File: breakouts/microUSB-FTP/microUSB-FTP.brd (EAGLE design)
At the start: 13.6 x 14.2 mm, 8 parts, among them X1 USB-MICROB

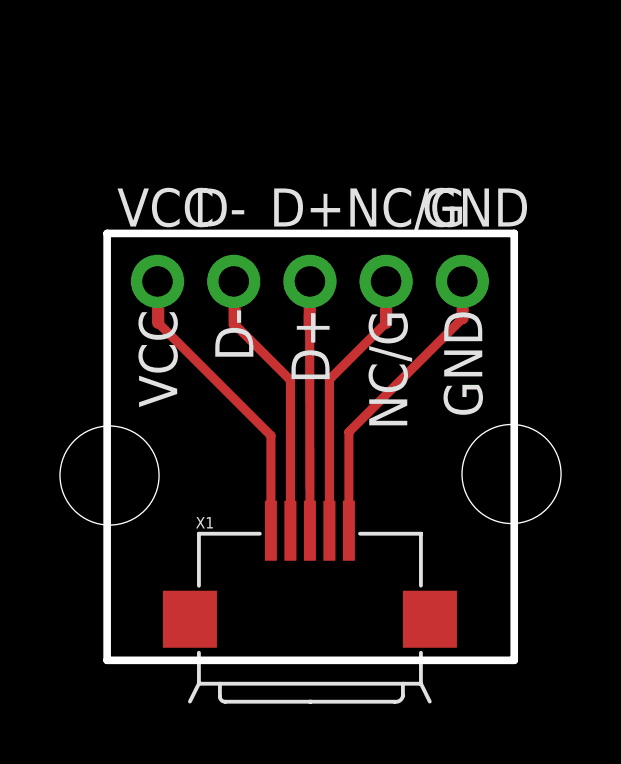
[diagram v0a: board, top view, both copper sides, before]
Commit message: microUSB FTP mid-point footprint
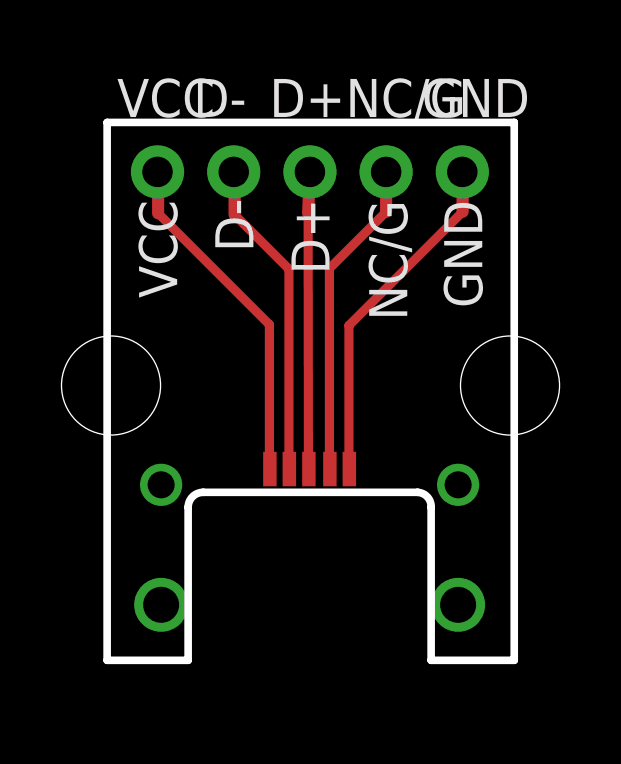
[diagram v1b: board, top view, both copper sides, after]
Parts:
- removed X1: USB-MICROB, SparkFun:USB-MICROB
- moved D+ 3.65 mm to (10.2, 16.3)
- moved D- 3.65 mm to (7.62, 16.3)
- moved GND 3.65 mm to (15.2, 16.3)
- moved NC/G 3.65 mm to (12.7, 16.3)
- moved VCC 3.65 mm to (5.08, 16.3)
- moved JP4 3.00 mm to (3.53, 9.21)
- moved JP3 2.95 mm to (16.8, 9.21)
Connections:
- net D+: no longer X1.D+
- net D-: no longer X1.D-
- net GND: no longer X1.GND
- net S$1: no longer X1.ID
- net VBUS: no longer X1.VBUS
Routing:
- net D+: track 8.31 -> 9.51 mm
- net D-: track 9.09 -> 10.3 mm
- net GND: track 9.88 -> 11.0 mm
- net S$1: track 9.09 -> 10.2 mm
- net VBUS: track 9.88 -> 11.0 mm
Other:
- board size 13.6 x 14.2 mm -> 13.6 x 17.9 mm
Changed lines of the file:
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@@
 <board>
 <plain>
-<wire x1="3.4" y1="0.05" x2="3.4" y2="14.28" width="0.254" layer="20"/>
-<wire x1="3.4" y1="14.28" x2="16.97" y2="14.28" width="0.254" layer="20"/>
-<wire x1="16.97" y1="14.28" x2="16.97" y2="0.05" width="0.254" layer="20"/>
-<wire x1="16.97" y1="0.05" x2="3.4" y2="0.05" width="0.254" layer="20"/>
-<text x="14.635" y="11.74" size="1.27" layer="121" font="vector" ratio="15" rot="R270">GND</text>
-<text x="9.545" y="11.79" size="1.27" layer="121" font="vector" ratio="15" rot="R270">D+</text>
-<text x="7.005" y="11.79" size="1.27" layer="121" font="vector" ratio="15" rot="R270">D-</text>
-<text x="4.465" y="11.74" size="1.27" layer="121" font="vector" ratio="15" rot="R270">VCC</text>
-<text x="12.135" y="11.74" size="1.27" layer="121" font="vector" ratio="15" rot="R270">NC/G</text>
-<text x="15" y="9.55" size="1.27" layer="122" font="vector" rot="MR0">quilix.com</text>
+<wire x1="3.4" y1="0.05" x2="3.4" y2="17.98" width="0.254" layer="20"/>
+<wire x1="3.4" y1="17.98" x2="16.97" y2="17.98" width="0.254" layer="20"/>
+<wire x1="16.97" y1="17.98" x2="16.97" y2="0.05" width="0.254" layer="20"/>
+<wire x1="16.97" y1="0.05" x2="14.2" y2="0.05" width="0.254" layer="20"/>
+<wire x1="14.2" y1="0.05" x2="14.2" y2="5.15" width="0.254" layer="20"/>
+<wire x1="14.2" y1="5.15" x2="13.75" y2="5.65" width="0.254" layer="20" curve="90"/>
+<wire x1="13.75" y1="5.65" x2="6.6" y2="5.65" width="0.254" layer="20"/>
+<wire x1="6.6" y1="5.65" x2="6.1" y2="5.15" width="0.254" layer="20" curve="90"/>
+<wire x1="6.1" y1="5.15" x2="6.1" y2="0.05" width="0.254" layer="20"/>
+<wire x1="6.1" y1="0.05" x2="3.4" y2="0.05" width="0.254" layer="20"/>
+<text x="14.635" y="15.39" size="1.27" layer="121" font="vector" ratio="15" rot="R270">GND</text>
+<text x="9.545" y="15.44" size="1.27" layer="121" font="vector" ratio="15" rot="R270">D+</text>
+<text x="7.005" y="15.44" size="1.27" layer="121" font="vector" ratio="15" rot="R270">D-</text>
+<text x="4.465" y="15.39" size="1.27" layer="121" font="vector" ratio="15" rot="R270">VCC</text>
+<text x="12.135" y="15.39" size="1.27" layer="121" font="vector" ratio="15" rot="R270">NC/G</text>
+<text x="14.85" y="12.95" size="1.27" layer="122" font="vector" rot="MR0">quilix.com</text>
+<rectangle x1="8.6" y1="5.85" x2="9.05" y2="7" layer="1"/>
+<rectangle x1="9.25" y1="5.85" x2="9.7" y2="7" layer="1"/>
+<rectangle x1="9.9" y1="5.85" x2="10.35" y2="7" layer="1"/>
+<rectangle x1="10.6" y1="5.85" x2="11.05" y2="7" layer="1"/>
+<rectangle x1="11.25" y1="5.85" x2="11.7" y2="7" layer="1"/>
+<rectangle x1="8.55" y1="5.8" x2="9.1" y2="7.05" layer="29"/>
+<rectangle x1="9.2" y1="5.8" x2="9.75" y2="7.05" layer="29"/>
+<rectangle x1="9.85" y1="5.8" x2="10.4" y2="7.05" layer="29"/>
+<rectangle x1="10.55" y1="5.8" x2="11.1" y2="7.05" layer="29"/>
+<rectangle x1="11.2" y1="5.8" x2="11.75" y2="7.05" layer="29"/>
 </plain>
 <attributes>
@@
 </autorouter>
 <elements>
-<element name="X1" library="SparkFun" package="USB-MICROB" value="USB-MICROB" x="10.16" y="1.27"/>
-<element name="JP3" library="SparkFun" package="STAND-OFF" value="STAND-OFF" x="16.88" y="6.26"/>
-<element name="JP4" library="SparkFun" package="STAND-OFF" value="STAND-OFF" x="3.48" y="6.21"/>
-<element name="VCC" library="adafruit" package="1X01-CLEANBIG" value="" x="5.08" y="12.68"/>
-<element name="D-" library="adafruit" package="1X01-CLEANBIG" value="" x="7.62" y="12.68"/>
-<element name="D+" library="adafruit" package="1X01-CLEANBIG" value="" x="10.16" y="12.68"/>
-<element name="NC/G" library="adafruit" package="1X01-CLEANBIG" value="" x="12.7" y="12.68"/>
-<element name="GND" library="adafruit" package="1X01-CLEANBIG" value="" x="15.24" y="12.68"/>
+<element name="JP3" library="SparkFun" package="STAND-OFF" value="STAND-OFF" x="16.83" y="9.21"/>
+<element name="JP4" library="SparkFun" package="STAND-OFF" value="STAND-OFF" x="3.53" y="9.21"/>
+<element name="VCC" library="adafruit" package="1X01-CLEANBIG" value="" x="5.08" y="16.33"/>
+<element name="D-" library="adafruit" package="1X01-CLEANBIG" value="" x="7.62" y="16.33"/>
+<element name="D+" library="adafruit" package="1X01-CLEANBIG" value="" x="10.16" y="16.33"/>
+<element name="NC/G" library="adafruit" package="1X01-CLEANBIG" value="" x="12.7" y="16.33"/>
+<element name="GND" library="adafruit" package="1X01-CLEANBIG" value="" x="15.24" y="16.33"/>
 </elements>
 <signals>
 <signal name="GND">
-<contactref element="X1" pad="GND"/>
 <contactref element="GND" pad="1"/>
-<wire x1="15.24" y1="12.68" x2="15.25" y2="12.67" width="0.4064" layer="1"/>
-<wire x1="15.25" y1="12.67" x2="15.25" y2="11.45" width="0.4064" layer="1"/>
-<wire x1="15.25" y1="11.45" x2="11.46" y2="7.66" width="0.3048" layer="1"/>
-<wire x1="11.46" y1="7.66" x2="11.46" y2="4.37" width="0.3048" layer="1"/>
+<wire x1="15.24" y1="16.33" x2="15.25" y2="16.32" width="0.4064" layer="1"/>
+<wire x1="15.25" y1="16.32" x2="15.25" y2="15" width="0.4064" layer="1"/>
+<wire x1="15.25" y1="15" x2="11.46" y2="11.21" width="0.3048" layer="1"/>
+<wire x1="11.46" y1="11.21" x2="11.46" y2="6.87" width="0.3048" layer="1"/>
 </signal>
 <signal name="D+">
-<contactref element="X1" pad="D+"/>
 <contactref element="D+" pad="1"/>
-<wire x1="10.16" y1="12.68" x2="10.15" y2="11.15" width="0.4064" layer="1"/>
-<wire x1="10.15" y1="11.15" x2="10.16" y2="4.37" width="0.3048" layer="1"/>
+<wire x1="10.16" y1="16.33" x2="10.1" y2="14.95" width="0.4064" layer="1"/>
+<wire x1="10.1" y1="14.95" x2="10.11" y2="6.82" width="0.3048" layer="1"/>
 </signal>
 <signal name="D-">
-<contactref element="X1" pad="D-"/>
 <contactref element="D-" pad="1"/>
-<wire x1="7.62" y1="12.68" x2="7.65" y2="12.65" width="0.4064" layer="1"/>
-<wire x1="7.65" y1="12.65" x2="7.65" y2="11.25" width="0.4064" layer="1"/>
-<wire x1="7.65" y1="11.25" x2="9.51" y2="9.39" width="0.3048" layer="1"/>
-<wire x1="9.51" y1="9.39" x2="9.51" y2="4.37" width="0.3048" layer="1"/>
+<wire x1="7.62" y1="16.33" x2="7.65" y2="16.3" width="0.4064" layer="1"/>
+<wire x1="7.65" y1="16.3" x2="7.65" y2="14.9" width="0.4064" layer="1"/>
+<wire x1="7.65" y1="14.9" x2="9.46" y2="13.09" width="0.3048" layer="1"/>
+<wire x1="9.46" y1="13.09" x2="9.46" y2="6.82" width="0.3048" layer="1"/>
 </signal>
 <signal name="VBUS">
-<contactref element="X1" pad="VBUS"/>
 <contactref element="VCC" pad="1"/>
-<wire x1="5.08" y1="12.68" x2="5.1" y2="12.66" width="0.4064" layer="1"/>
-<wire x1="5.1" y1="12.66" x2="5.1" y2="11.3" width="0.4064" layer="1"/>
-<wire x1="5.1" y1="11.3" x2="8.86" y2="7.54" width="0.3048" layer="1"/>
-<wire x1="8.86" y1="7.54" x2="8.86" y2="4.37" width="0.3048" layer="1"/>
+<wire x1="5.08" y1="16.33" x2="5.1" y2="16.31" width="0.4064" layer="1"/>
+<wire x1="5.1" y1="16.31" x2="5.1" y2="14.95" width="0.4064" layer="1"/>
+<wire x1="5.1" y1="14.95" x2="8.81" y2="11.24" width="0.3048" layer="1"/>
+<wire x1="8.81" y1="11.24" x2="8.81" y2="6.87" width="0.3048" layer="1"/>
 </signal>
 <signal name="S$1">
 <contactref element="NC/G" pad="1"/>
-<contactref element="X1" pad="ID"/>
-<wire x1="12.7" y1="12.68" x2="12.7" y2="11.3" width="0.4064" layer="1"/>
-<wire x1="12.7" y1="11.3" x2="10.81" y2="9.41" width="0.3048" layer="1"/>
-<wire x1="10.81" y1="9.41" x2="10.81" y2="4.37" width="0.3048" layer="1"/>
+<wire x1="12.7" y1="16.33" x2="12.7" y2="15" width="0.4064" layer="1"/>
+<wire x1="12.7" y1="15" x2="10.81" y2="13.11" width="0.3048" layer="1"/>
+<wire x1="10.81" y1="13.11" x2="10.81" y2="6.87" width="0.3048" layer="1"/>
+</signal>
+<signal name="S$2">
+<via x="15.1" y="1.9" extent="1-16" drill="1.2"/>
+<via x="5.2" y="1.9" extent="1-16" drill="1.2"/>
+</signal>
+<signal name="S$3">
+<via x="15.1" y="5.9" extent="1-16" drill="0.9"/>
+<via x="5.2" y="5.9" extent="1-16" drill="0.9"/>
 </signal>
 </signals>
